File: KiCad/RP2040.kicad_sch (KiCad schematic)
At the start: 25 parts, among them J1 Button, J2 Conn_01x03, J3 Button, U3 RP2040, Y1 3225_4P 12MHz

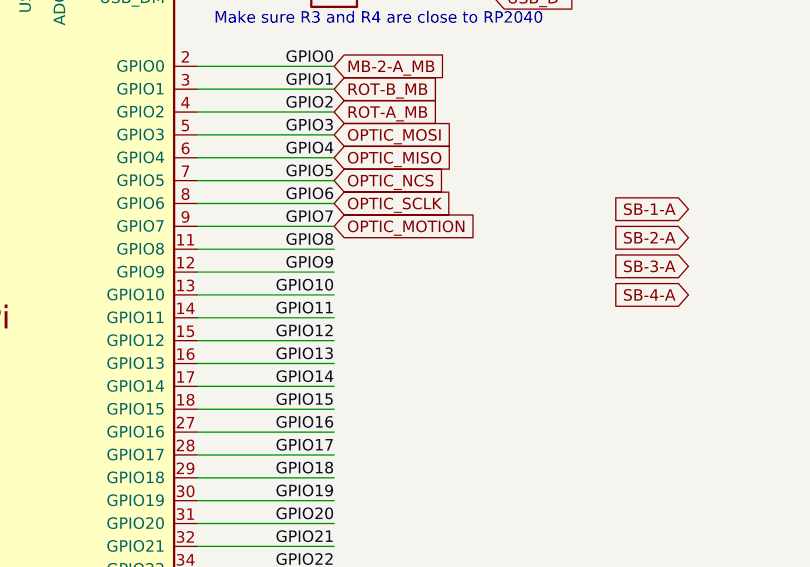
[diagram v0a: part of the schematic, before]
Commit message: Added missing connections.
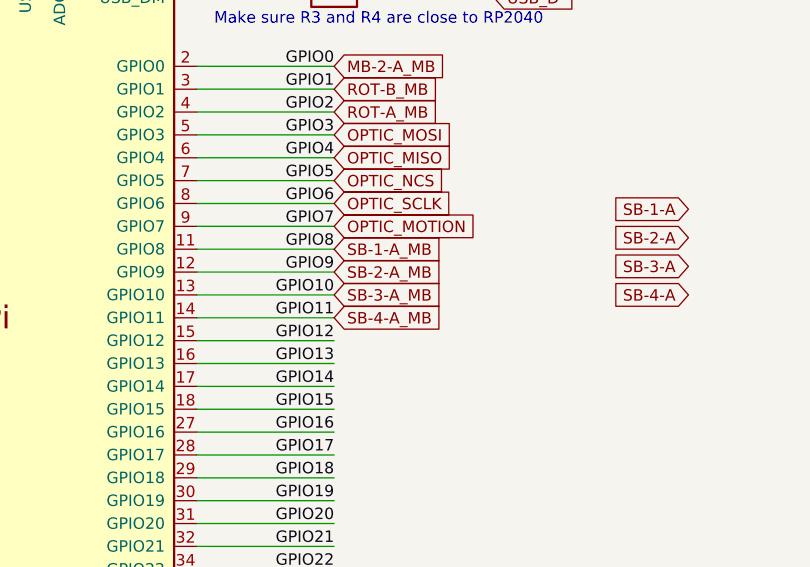
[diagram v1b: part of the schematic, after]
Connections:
- net GPIO10 renamed SB-3-A_MB
- net GPIO11 renamed SB-4-A_MB
- net GPIO8 renamed SB-1-A_MB
- net GPIO9 renamed SB-2-A_MB
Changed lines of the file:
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@@
+    )
+  )
+  (global_label "SB-3-A_MB" (shape input) (at 212.09 101.6 0) (fields_autoplaced)
+    (effects (font (size 1.27 1.27)) (justify left))
+    (property "Intersheetrefs" "${INTERSHEET_REFS}" (at 226.7817 101.6 0)
+      (effects (font (size 1.27 1.27)) (justify left) hide)
     )
   )
@@
     (effects (font (size 1.27 1.27)) (justify left))
     (property "Intersheetrefs" "${INTERSHEET_REFS}" (at 225.1904 78.74 0)
+      (effects (font (size 1.27 1.27)) (justify left) hide)
+    )
+  )
+  (global_label "SB-2-A_MB" (shape input) (at 212.09 99.06 0) (fields_autoplaced)
+    (effects (font (size 1.27 1.27)) (justify left))
+    (property "Intersheetrefs" "${INTERSHEET_REFS}" (at 226.7817 99.06 0)
       (effects (font (size 1.27 1.27)) (justify left) hide)
     )
@@
       (effects (font (size 1.27 1.27)) (justify left) hide)
     )
+  )
+  (global_label "SB-4-A_MB" (shape input) (at 212.09 104.14 0) (fields_autoplaced)
+    (effects (font (size 1.27 1.27)) (justify left))
+    (property "Intersheetrefs" "${INTERSHEET_REFS}" (at 226.7817 104.14 0)
+      (effects (font (size 1.27 1.27)) (justify left) hide)
+    )
+  )
+  (global_label "SB-1-A_MB" (shape input) (at 212.09 96.52 0) (fields_autoplaced)
+    (effects (font (size 1.27 1.27)) (justify left))
+    (property "Intersheetrefs" "${INTERSHEET_REFS}" (at 226.7817 96.52 0)
+      (effects (font (size 1.27 1.27)) (justify left) hide)
+    )

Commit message: double checked board and tidied things up.
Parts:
- R10, R9: value 27Ohms 0402 Resistor -> 27Ohms 0402 Resistor

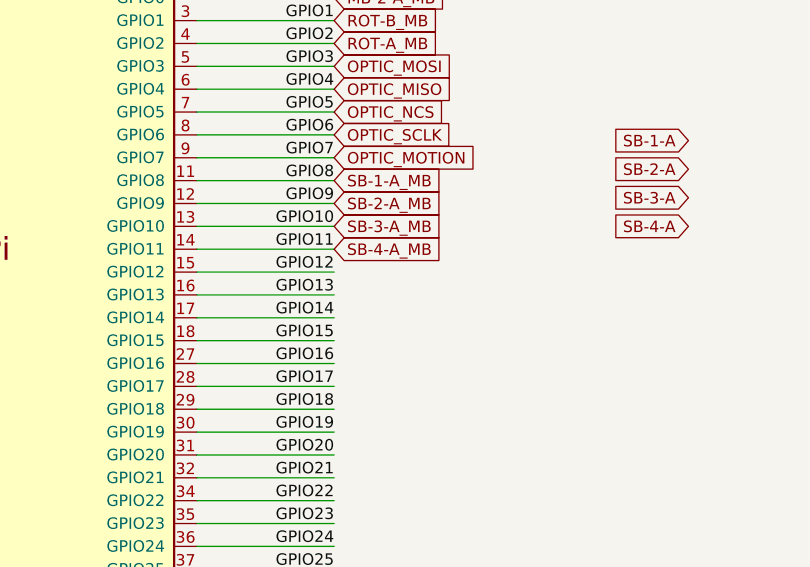
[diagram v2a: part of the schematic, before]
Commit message: downsized main board, added more buttons and respective connector, improved spacing of various power traces
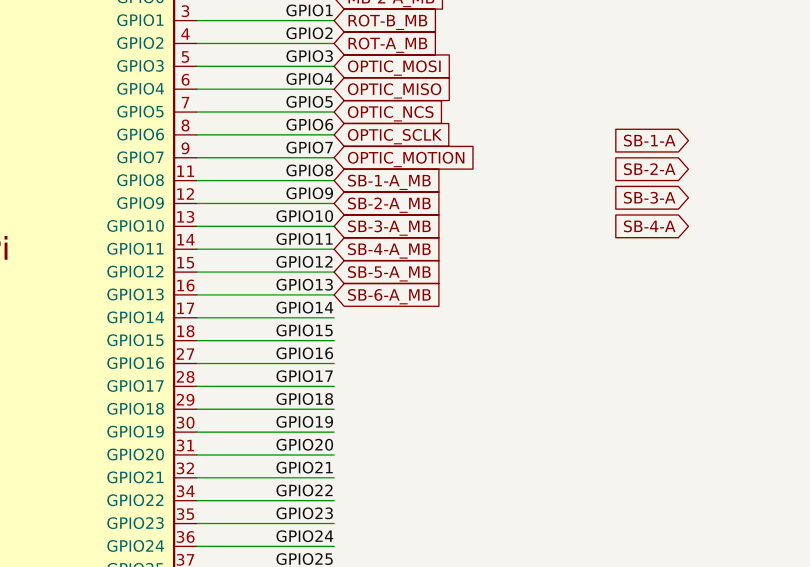
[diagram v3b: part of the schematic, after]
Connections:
- net GPIO12 renamed SB-5-A_MB
- net GPIO13 renamed SB-6-A_MB
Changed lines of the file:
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@@
+		)
+	)
+	(global_label "SB-6-A_MB"
+		(shape input)
+		(at 212.09 109.22 0)
+		(fields_autoplaced yes)
+		(effects
+			(font
+				(size 1.27 1.27)
+			)
+			(justify left)
+		)
+		(property "Intersheetrefs" "${INTERSHEET_REFS}"
+			(at 226.7817 109.22 0)
+			(effects
+				(font
+					(size 1.27 1.27)
+				)
+				(justify left)
+				(hide yes)
+			)
 		)
 	)
@@
 			(effects
 				(font
+					(size 1.27 1.27)
+				)
+				(justify left)
+				(hide yes)
+			)
+		)
+	)
+	(global_label "SB-5-A_MB"
+		(shape input)
+		(at 212.09 106.68 0)
+		(fields_autoplaced yes)
+		(effects
+			(font
+				(size 1.27 1.27)
+			)
+			(justify left)
+		)
+		(property "Intersheetrefs" "${INTERSHEET_REFS}"
+			(at 226.7817 106.68 0)
+			(effects
+				(font

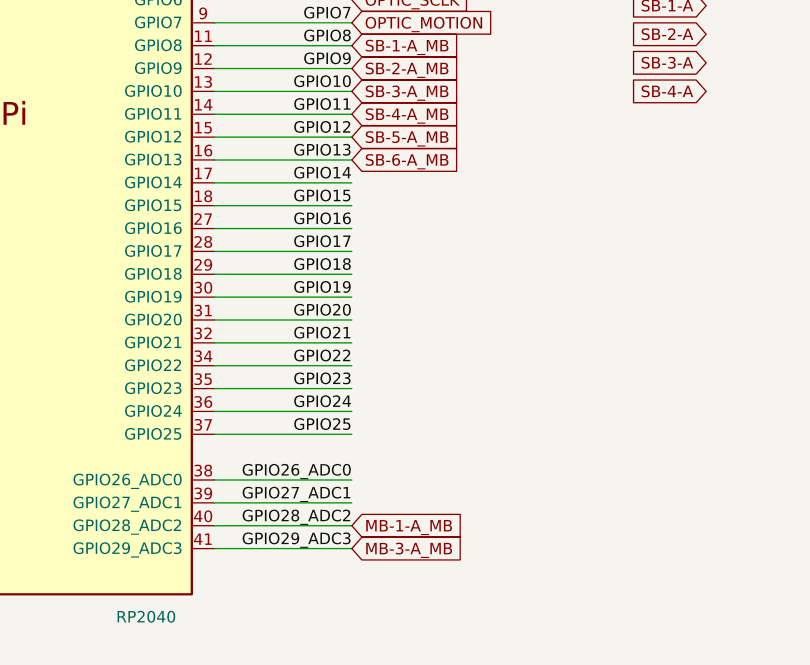
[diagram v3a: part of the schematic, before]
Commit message: added header for unused GPIOs
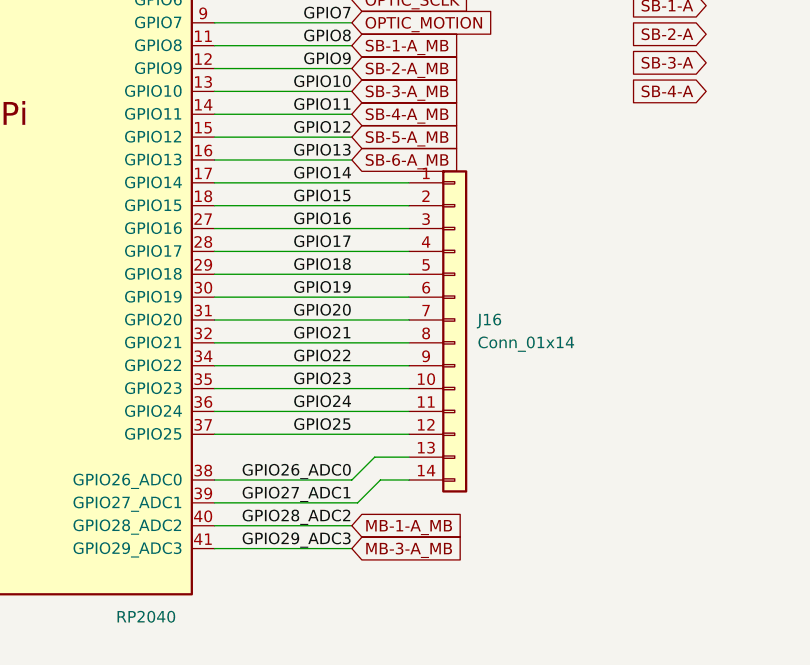
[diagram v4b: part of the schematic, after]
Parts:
- added J16: Conn_01x14, Connector_PinHeader_1.00mm:PinHeader_1x14_P1.00mm_Vertical, symbol Connector_Generic:Conn_01x14
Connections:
- net GPIO14: now also J16.1 (Pin_1)
- net GPIO15: now also J16.2 (Pin_2)
- net GPIO16: now also J16.3 (Pin_3)
- net GPIO17: now also J16.4 (Pin_4)
- net GPIO18: now also J16.5 (Pin_5)
- net GPIO19: now also J16.6 (Pin_6)
- net GPIO20: now also J16.7 (Pin_7)
- net GPIO21: now also J16.8 (Pin_8)
- net GPIO22: now also J16.9 (Pin_9)
- net GPIO23: now also J16.10 (Pin_10)
- net GPIO24: now also J16.11 (Pin_11)
- net GPIO25: now also J16.12 (Pin_12)
- net GPIO26_ADC0: now also J16.13 (Pin_13)
- net GPIO27_ADC1: now also J16.14 (Pin_14)

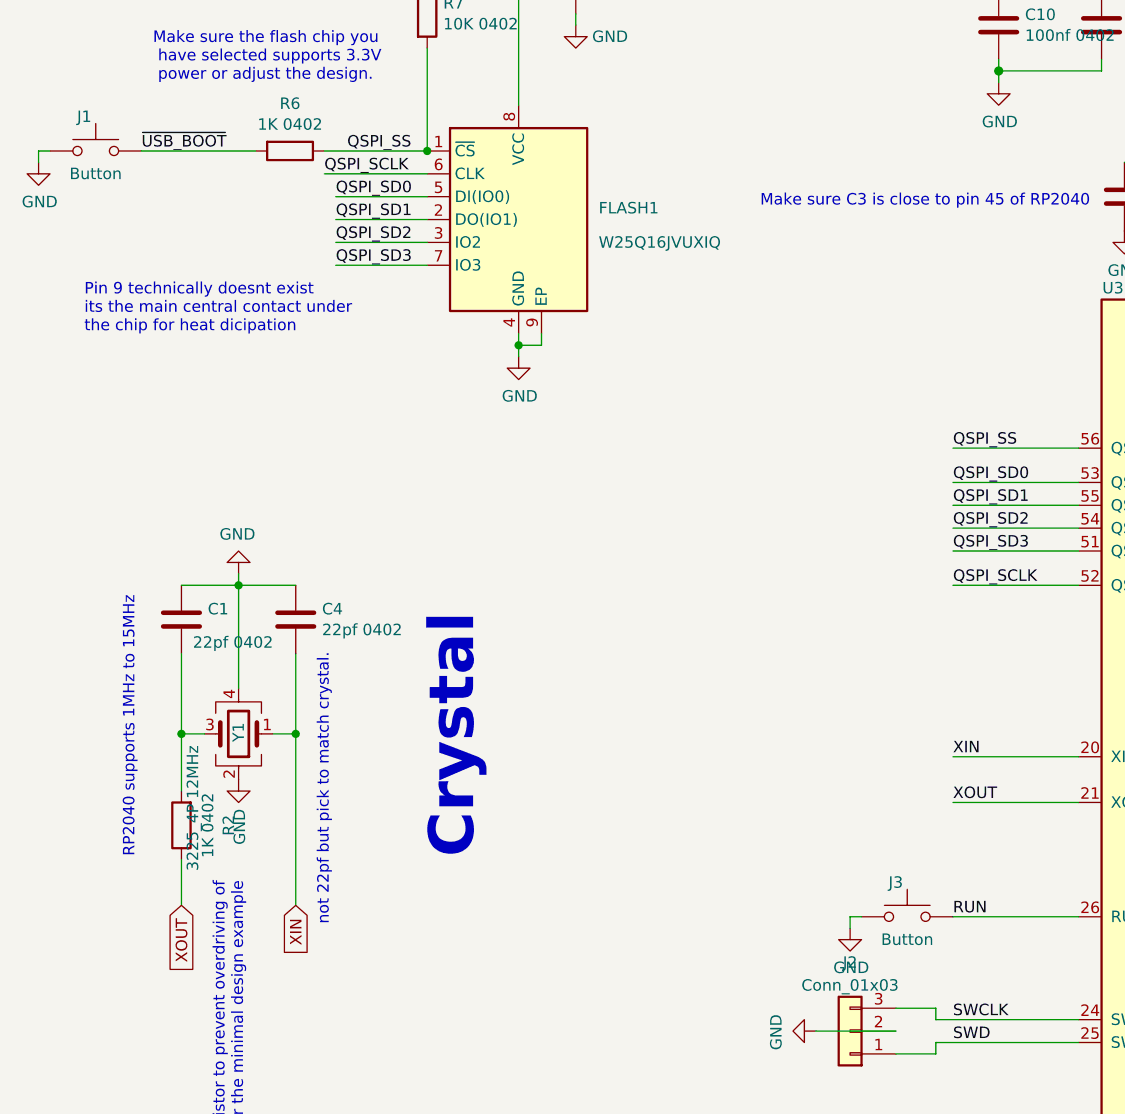
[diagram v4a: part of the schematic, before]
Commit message: updated part values, generated production files
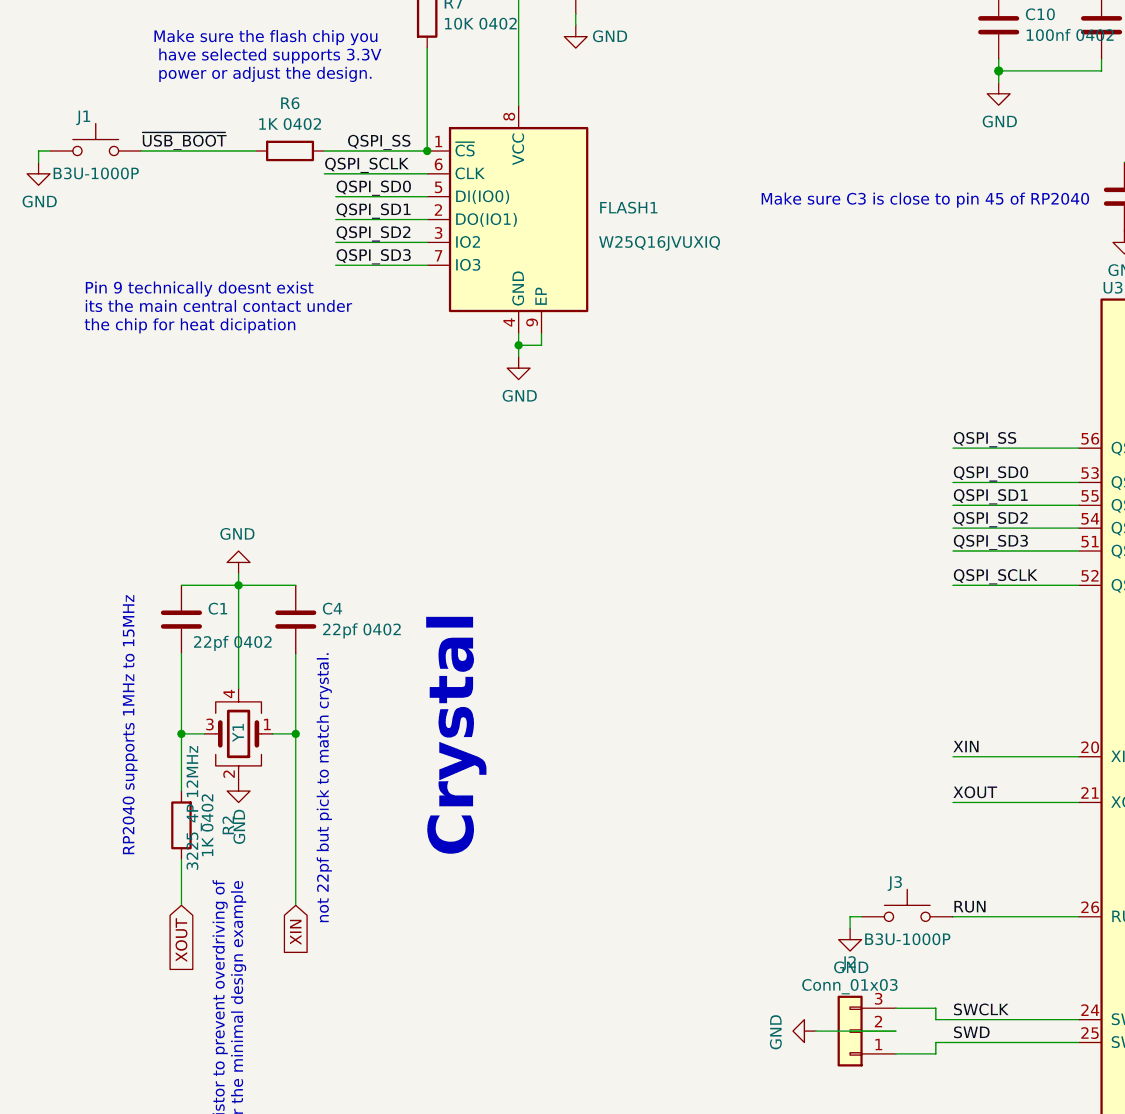
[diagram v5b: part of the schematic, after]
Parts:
- J1, J3: value Button -> B3U-1000P
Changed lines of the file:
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@@
 			)
 		)
-		(property "Value" "Button"
+		(property "Value" "B3U-1000P"
 			(at 24.13 46.99 0)
 			(effects
@@
 			)
 		)
-		(property "Value" "Button"
+		(property "Value" "B3U-1000P"
 			(at 114.3 132.08 0)
 			(effects
